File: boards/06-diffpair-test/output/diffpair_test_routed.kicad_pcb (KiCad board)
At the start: 4 copper layers, 100 x 80 mm, 7 parts, among them J1 USB-C, J3 MiniPCIe, J4 FFC4, U1 QFN32_USB2, U2 BGA49_USB3, U3 QFP48_PCIe, U4 QFN24_MIPI

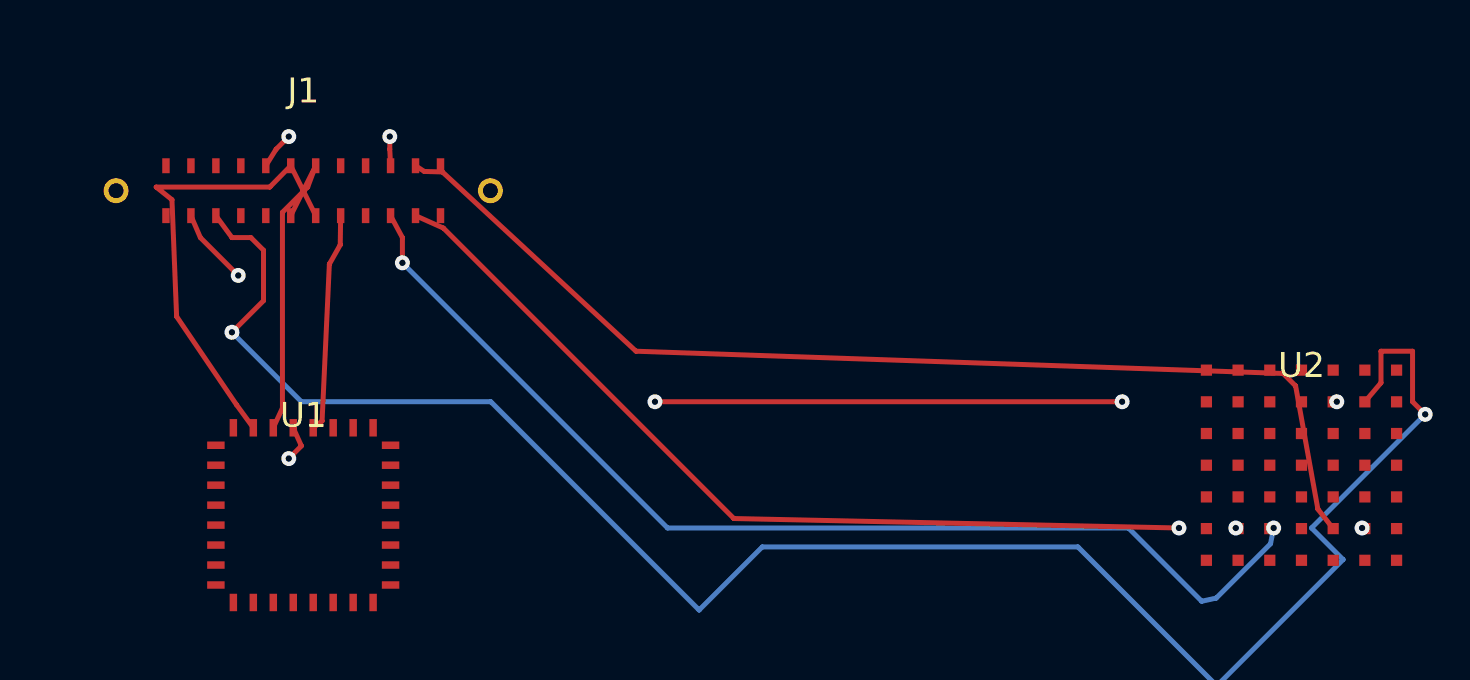
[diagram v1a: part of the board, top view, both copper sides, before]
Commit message: test(router): add coverage for skipped-pour-net pad clearance + regen board 06 PCB
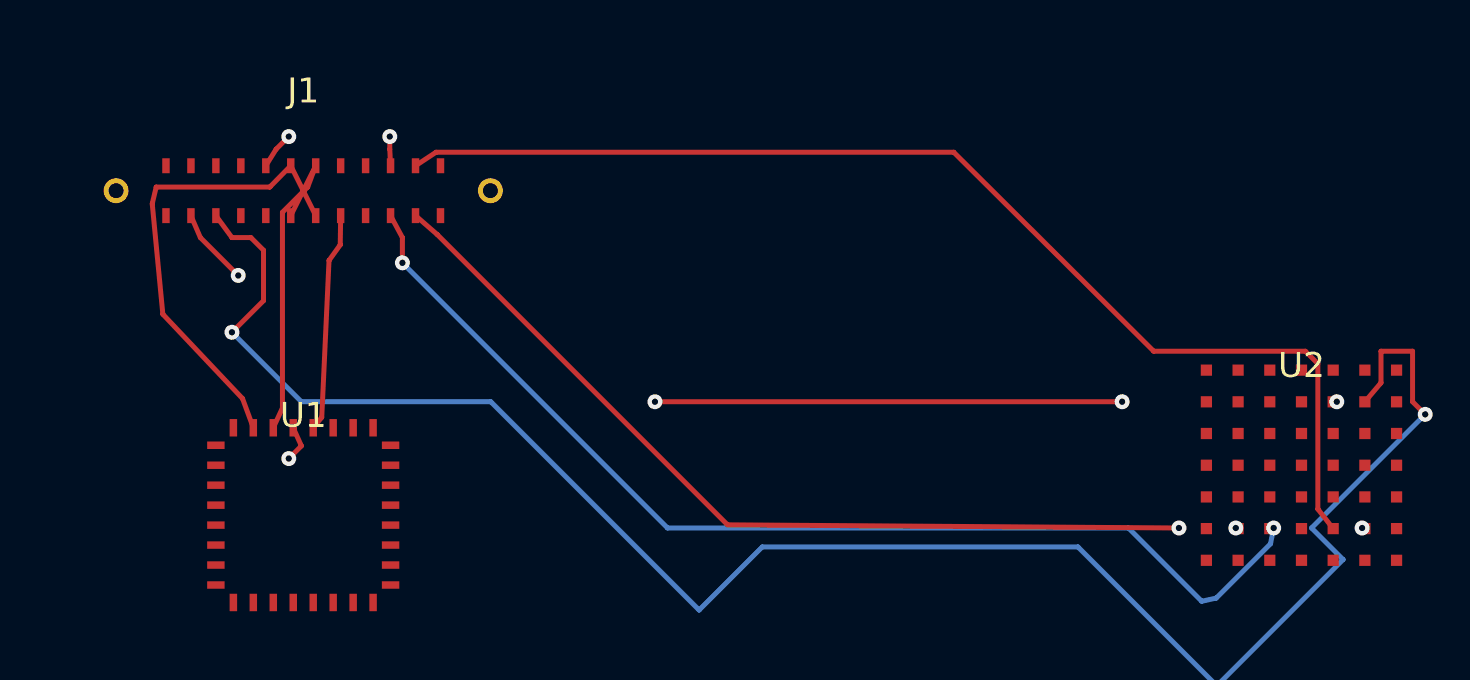
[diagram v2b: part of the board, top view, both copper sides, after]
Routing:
- net USB3_RX2+: track 44.4 -> 46.6 mm
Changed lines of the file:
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@@
 	(segment
 		(start 109.1074 108.8544)
-		(end 109.7398 109.3603)
+		(end 108.9494 109.5216)
 		(width 0.2)
 		(layer "F.Cu")
@@
 	)
 	(segment
-		(start 109.7398 109.3603)
-		(end 109.9262 114.0405)
+		(start 108.9494 109.5216)
+		(end 109.3744 113.9489)
 		(width 0.2)
 		(layer "F.Cu")
@@
 	)
 	(segment
-		(start 109.9262 114.0405)
-		(end 112.3295 117.5823)
+		(start 109.3744 113.9489)
+		(end 112.5681 117.3293)
 		(width 0.2)
 		(layer "F.Cu")
@@
 	)
 	(segment
-		(start 112.3295 117.5823)
+		(start 112.5681 117.3293)
 		(end 113.0000 118.5000)
 		(width 0.2)
@@
 	(segment
 		(start 119.5000 110.0000)
-		(end 120.6180 110.4988)
-		(width 0.2)
-		(layer "F.Cu")
-		(net 12)
-	)
-	(segment
-		(start 120.6180 110.4988)
-		(end 132.2552 122.1360)
-		(width 0.2)
-		(layer "F.Cu")
-		(net 12)
-	)
-	(segment
-		(start 132.2552 122.1360)
+		(end 120.3651 110.7517)
+		(width 0.2)
+		(layer "F.Cu")
+		(net 12)
+	)
+	(segment
+		(start 120.3651 110.7517)
+		(end 132.0023 122.3889)
+		(width 0.2)
+		(layer "F.Cu")
+		(net 12)
+	)
+	(segment
+		(start 132.0023 122.3889)
 		(end 150.0905 122.5154)
 		(width 0.2)
@@
 	(segment
 		(start 119.5000 108.0000)
-		(end 119.8517 108.2290)
-		(width 0.2)
-		(layer "F.Cu")
-		(net 14)
-	)
-	(segment
-		(start 119.8517 108.2290)
-		(end 120.5772 108.2484)
-		(width 0.2)
-		(layer "F.Cu")
-		(net 14)
-	)
-	(segment
-		(start 120.5772 108.2484)
-		(end 128.3340 115.4319)
-		(width 0.2)
-		(layer "F.Cu")
-		(net 14)
-	)
-	(segment
-		(start 128.3340 115.4319)
-		(end 154.2647 116.3233)
-		(width 0.2)
-		(layer "F.Cu")
-		(net 14)
-	)
-	(segment
-		(start 154.2647 116.3233)
-		(end 154.7647 116.8233)
-		(width 0.2)
-		(layer "F.Cu")
-		(net 14)
-	)
-	(segment
-		(start 154.7647 116.8233)
+		(end 120.3214 107.4586)
+		(width 0.2)
+		(layer "F.Cu")
+		(net 14)
+	)
+	(segment
+		(start 120.3214 107.4586)
+		(end 141.0659 107.4586)
+		(width 0.2)
+		(layer "F.Cu")
+		(net 14)
+	)
+	(segment
+		(start 141.0659 107.4586)
+		(end 149.0785 115.4319)
+		(width 0.2)
+		(layer "F.Cu")
+		(net 14)
+	)
+	(segment
+		(start 149.0785 115.4319)
+		(end 155.1561 115.4319)
+		(width 0.2)
+		(layer "F.Cu")
+		(net 14)
+	)
+	(segment
+		(start 155.1561 115.4319)
+		(end 155.6561 115.9319)
+		(width 0.2)
+		(layer "F.Cu")
+		(net 14)
+	)
+	(segment
+		(start 155.6561 115.9319)
 		(end 155.6561 121.7565)
 		(width 0.2)
@@
 	(segment
 		(start 116.4826 111.1699)
-		(end 116.0467 111.9439)
+		(end 116.0337 111.7952)
 		(width 0.2)
 		(layer "F.Cu")
@@
 	)
 	(segment
-		(start 116.0467 111.9439)
-		(end 115.7550 118.2297)
+		(start 116.0337 111.7952)
+		(end 115.7419 118.0810)
 		(width 0.2)
 		(layer "F.Cu")
@@
 	)
 	(segment
-		(start 115.7550 118.2297)
+		(start 115.7419 118.0810)
 		(end 115.4000 118.5000)
 		(width 0.2)
